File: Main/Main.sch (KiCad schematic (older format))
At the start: 63 parts, among them J1 Power, J2 ModeSW, J3 SGND, J4 -5V, J5 MA1M→, J6 LFO_out, J7 →MA1M, U1 LA6358-2, U2 NE556, U3 NJM4556-1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

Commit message: update LFO design
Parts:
- added C? (x2): 100µF, symbol CP
- added D? (x2): 5V1, symbol D_Zener
- added J?: LFO_trim, symbol CONN_01X01
- J6: value LFO_out -> LFO_full
- R10: value 470K -> 1M
- R12: value 470K -> 100K
- R13: value 10K -> 150K
- R23: value 82K -> 56K
- R8: value 330 -> 120
- renumbered GlobLFO_Amt1 to GlobLFO_Trim1
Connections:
- net LFO_fq_return is gone; now on net LFO_fq_ret: R11.2
- net GND: now also C?.1, D?.1 (K)
- net LFO_fq_send: now also R12.1, U3.1; no longer C9.1, R11.1, U3.3 (+)
- net LFO→Trim: now reaches J6.1 (P1), U4.1, U4.2 (-)
- net LFO→Trim: now also GlobLFO_Trim1.3; no longer FiltSelM1.14
- net at C8.1, D5.2 (A): now also R8.1; no longer R8.2
- net -11V renamed -10V
- net -10V: now also R8.2, C?.2, D?.2 (A); no longer R8.1
- net 11V renamed 10V
- net 10V: now also C?.1, D?.1 (K)
- net LFO_shape_ret renamed TRI_shape_ret
- removed net LFO_shape_send: LFO_shape1.1, R12.1, U3.1
- net LFO→buf: no longer names the net of U4.3 (+)
- net LFO→buf: now also D9.2 (A), R13.1; no longer GlobLFO_Trim1.3
- removed net LFO→trim: D9.2 (A), GlobLFO_Trim1.2, R13.1
- new net: FiltSelM1.14, GlobLFO_Trim1.2, J?.1 (P1)
- new net: C?.2, D?.2 (A)
- new net TRI_shape_send: C9.1, LFO_shape1.1, R11.1, U3.3 (+)
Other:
- note added: "(-10V not to be \nused externally)"
- note added: "(10V not to be \nused externally)"
- note added: "(pre-trimmer)"
- note added: "Add LFO to Melody\nPitch Toggle and try\nsome kind of course\ntuning control."
- note added: "Global LFO"
- note added: "Off-PCB Point to Point Wired Panel"
- note added: "Output Buffer"
- note added: "Squ/Tri Osc"
- note added: "The lowest voltage\nwe'll see here is \n10.13V (powered\nby 6 NiMH AA)"
- note added: "ToDo:"
- note added: "Tri→Squ Shaper"
- note added: "\----- Global LFO Panel Controls -------/"
- note added: "\-------------- Main (Melody) Filter Panel Controls ---------------/"
- note removed: "(-11V not to be \nused externally)"
- note removed: "Global LFO \nInput Buffer"
- note removed: "LFO Buffer"
- note removed: "LFO Generator"
- note removed: "LFO Shaper"
- note removed: "Main Panel (Off-PCB Point to Point Wiring)"
- moved on the sheet: C10, C2, C3, C4, C5, C6, C7, C8, C9, D1, D2, D3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

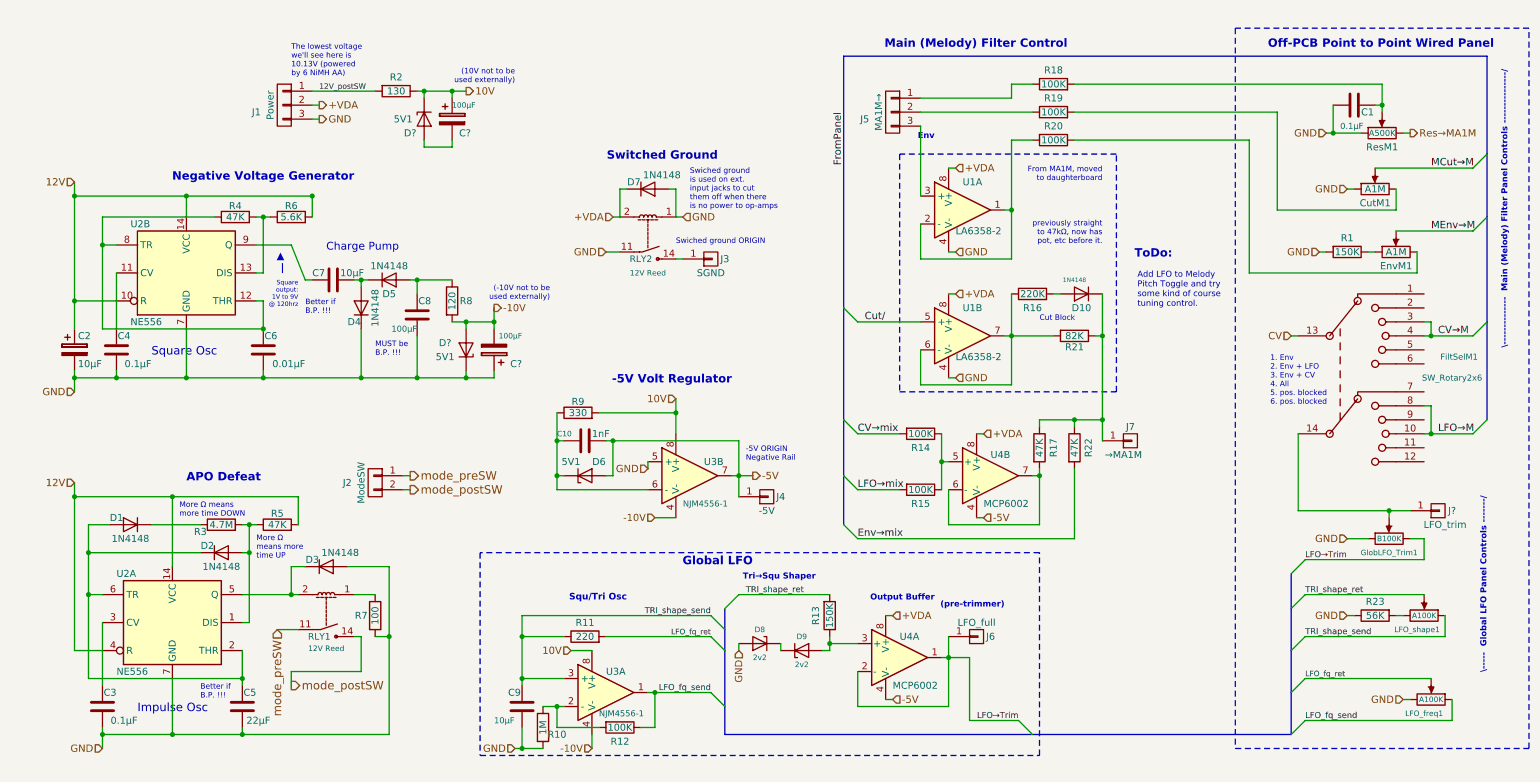
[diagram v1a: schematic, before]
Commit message: updating with modularized version
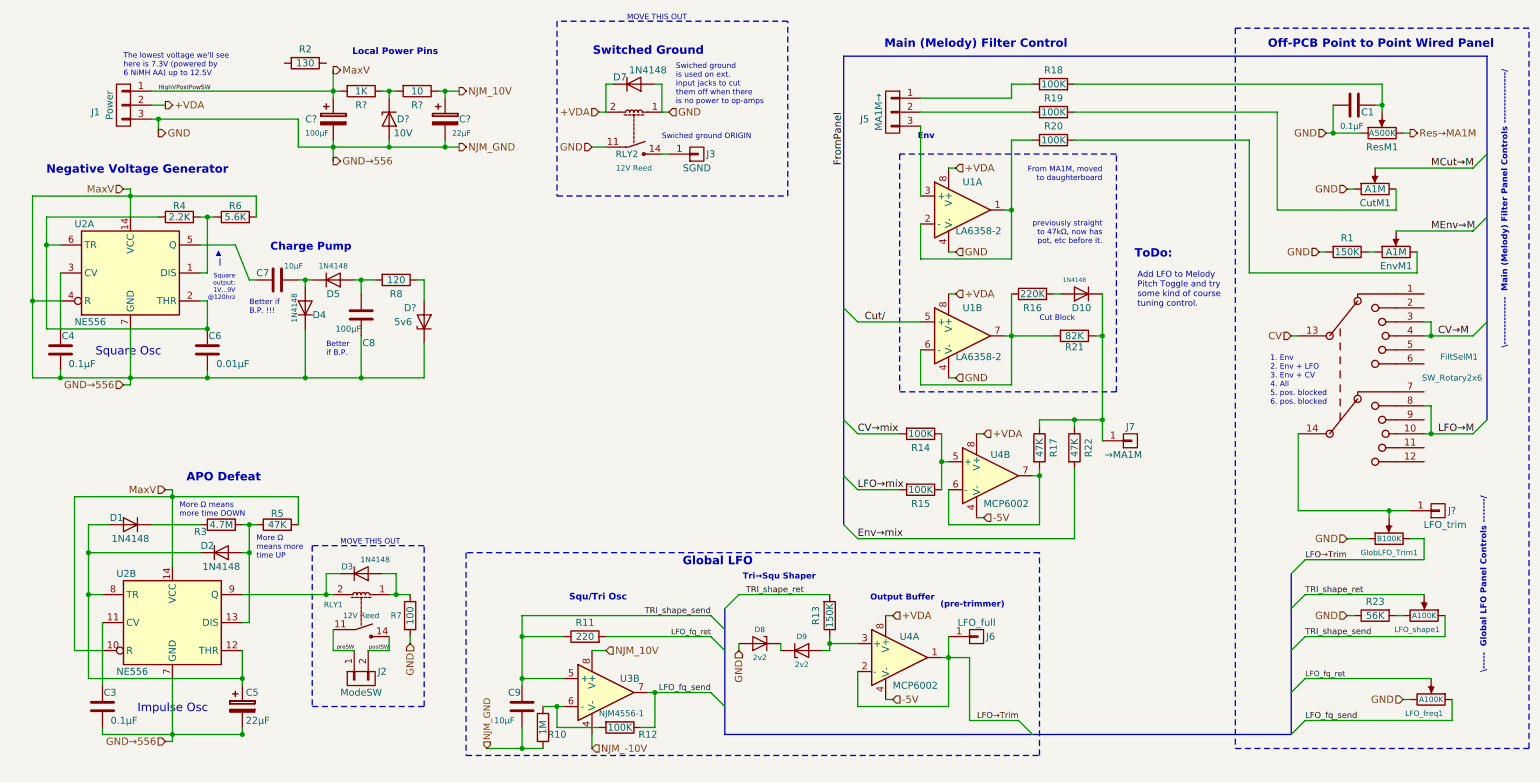
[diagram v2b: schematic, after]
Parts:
- removed C10: 1nF, symbol C
- removed C2: 10µF, symbol CP
- removed C5: 22µF, symbol C
- removed C?: 100µF, symbol CP
- removed D6: 5V1, symbol D_Zener
- removed J4: -5V, symbol CONN_01X01
- removed R9: 330, symbol R
- removed unit 1 of U3
- added C5, C?: 22µF, symbol CP
- added R?: 1K, symbol R
- added R?: 10, symbol R
- D?: value 5V1 -> 10V
- D?: value 5V1 -> 5v6
- R4: value 47K -> 2.2K
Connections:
- net 12V is gone; now on net GND: R5.2, R6.2, U2.10 (R), U2.14 (VCC), U2.14 (VCC), U2.4 (R)
- net -5V: no longer U3.7
- net GND: now also C?.1, C?.2, D?.2 (A), J1.1 (P1), C5.2, C?.2, R?.2; no longer D3.2 (A), U3.5 (+)
- net LFO_fq_send: now also U3.7
- net TRI_shape_send: now also U3.5 (+)
- net at R4.2, R6.1: now also U2.1 (DIS); no longer U2.13 (DIS)
- net at C8.1, D5.2 (A): now also R8.2; no longer R8.1
- net at C6.1, R4.1: now also U2.2 (THR), U2.6 (TR); no longer U2.12 (THR), U2.8 (TR)
- net at C4.1: now also U2.3 (CV); no longer U2.11 (CV)
- net at D2.2 (A), R3.2, R5.1: now also U2.13 (DIS); no longer U2.1 (DIS)
- net at D1.2 (A), D2.1 (K): now also U2.12 (THR), U2.8 (TR), C5.1; no longer U2.2 (THR), U2.6 (TR)
- net at U2.9 (Q): now also D3.1 (K), RLY1.2; no longer C7.2
- net at C3.1: now also U2.11 (CV); no longer U2.3 (CV)
- net at R7.1, RLY1.1: now also D3.2 (A)
- net at R10.1, R12.2: now also U3.6 (-)
- removed net -10V: D?.2 (A), R8.2, U3.4 (V-)
- removed net 10V: C?.1, D?.1 (K), R2.1, U3.8 (V+)
- net 12V_postSW: no longer names the net of R2.2
- net 12V_postSW: no longer J1.1 (P1)
- net mode_postSW renamed postSW
- net mode_preSW renamed preSW
- new net: C7.2, U2.5 (Q)
- new net: D?.1 (K), R?.1, R?.2
- new net: D?.2 (A), R8.1
- new net NJM_-10V: U3.4 (V-)
- new net NJM_10V: C?.1, R?.1, U3.8 (V+)
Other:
- note added: "Better\nif B.P.\n"
- note added: "Local Power Pins"
- note added: "MOVE THIS OUT"
- note added: "Square \noutput: \n1V...9V\n@120hrz"
- note added: "The lowest voltage we'll see \nhere is 7.3V (powered by \n6 NiMH AA) up to 12.5V"
- note removed: "(-10V not to be \nused externally)"
- note removed: "(10V not to be \nused externally)"
- note removed: "-5V ORIGIN\nNegative Rail"
- note removed: "-5V Volt Regulator"
- note removed: "MUST be\nB.P. !!!\n"
- note removed: "Square \noutput: \n1V to 9V\n@ 120hrz"
- note removed: "The lowest voltage\nwe'll see here is \n10.13V (powered\nby 6 NiMH AA)"
- moved on the sheet: C4, C6, C7, C8, C?, D3, D4, D5, D7, D?, J1, J2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
